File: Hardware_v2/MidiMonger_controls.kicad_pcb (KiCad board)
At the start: 2 copper layers, 40 x 110 mm, 31 parts, among them J10 Gate8_Out, J11 CV1_Out, J12 CV2_Out, J13 CV3_Out, J14 CV4_Out, J15 USB_B_Wurth, J16 MIDI_DIN, J2 Gate3_Out, J20 Conn_01x09_Female, J21 Conn_01x08_Female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

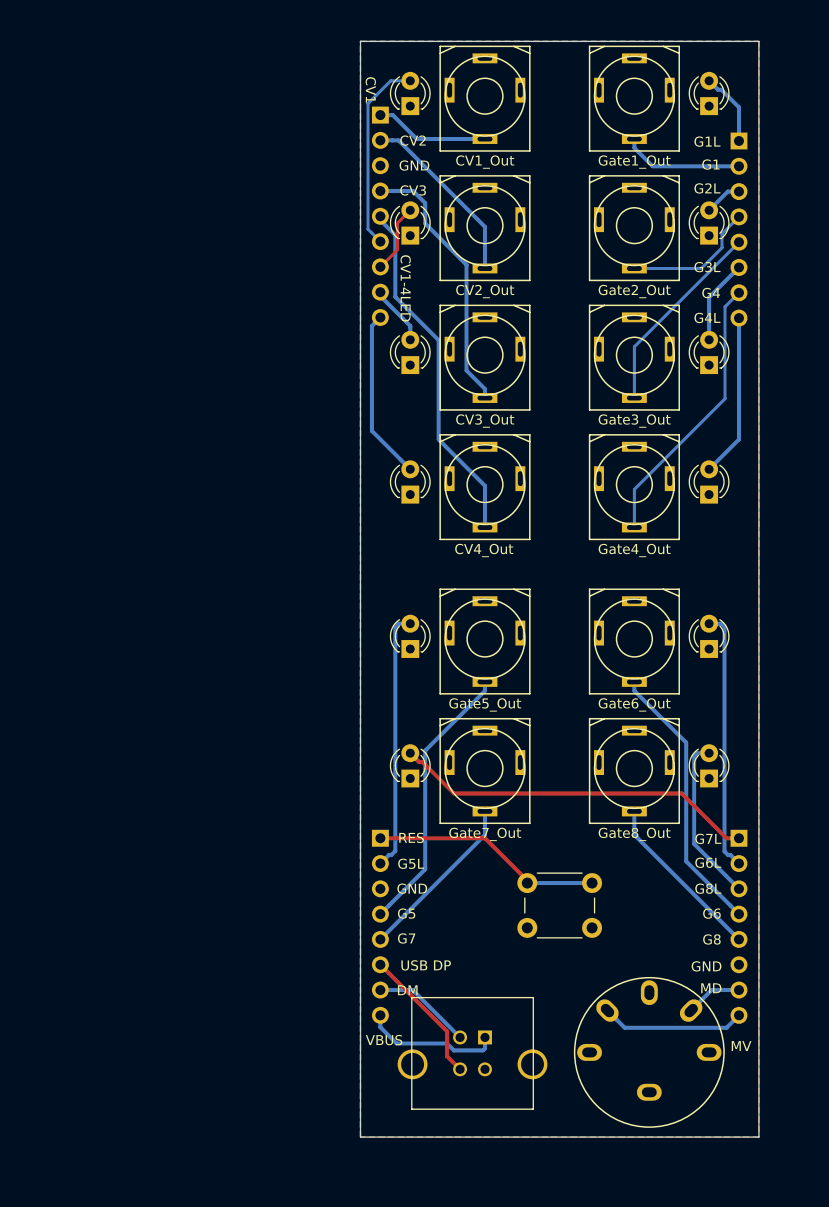
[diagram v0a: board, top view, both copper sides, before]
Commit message: Started Control layout
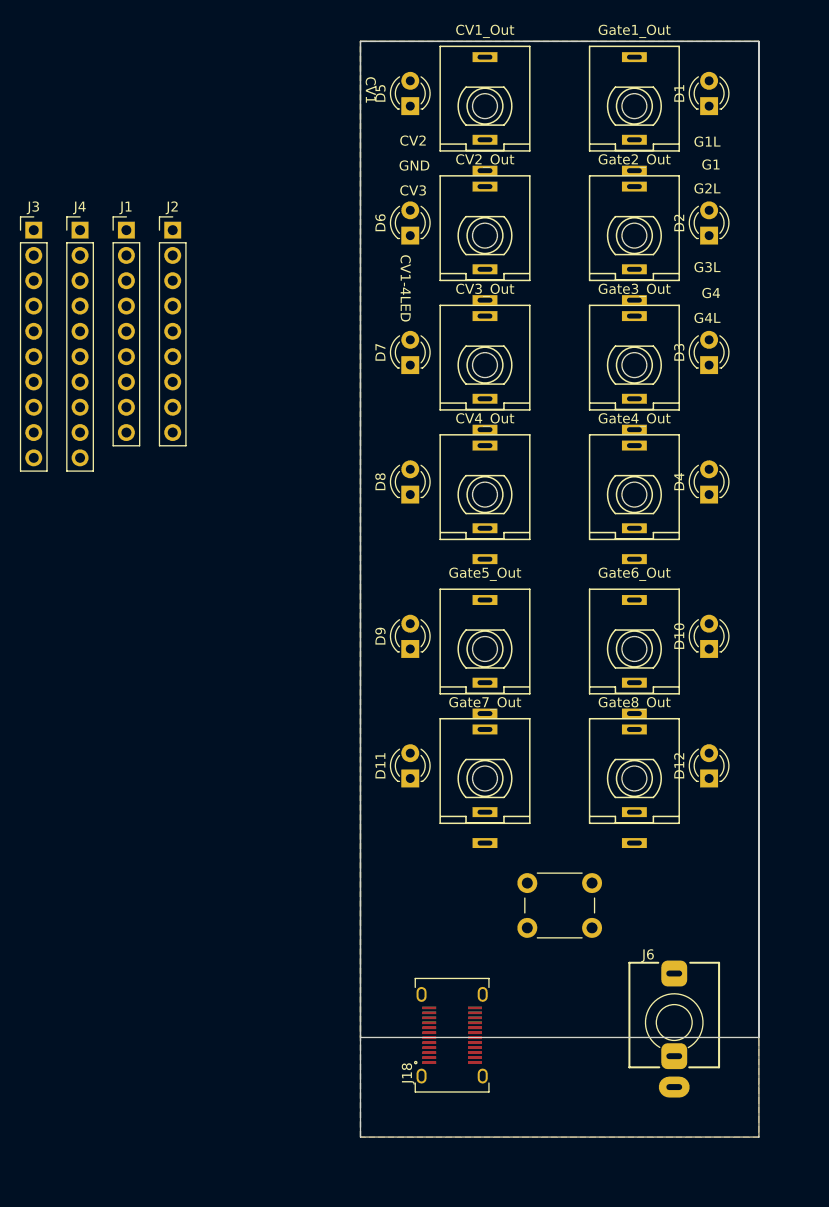
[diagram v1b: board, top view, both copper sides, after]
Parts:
- removed the J15 at (108.5, 140.0)
- removed the J16 at (125.0, 135.5)
- removed J20: Conn_01x09_Female, Socket_Strips:Socket_Strip_Straight_1x09_Pitch2.54mm
- removed J21, J22, J23: Conn_01x08_Female, Socket_Strips:Socket_Strip_Straight_1x08_Pitch2.54mm
- added J1: Conn_01x09_Male, Connector_PinHeader_2.54mm:PinHeader_1x09_P2.54mm_Vertical, F.Cu at (72.5, 59.0)
- added J18: USB_C_Receptacle, Custom_Footprints:USB_C_Receptacle_Amphenol_12401951E412A, F.Cu at (105.2, 139.8)
- added J2: Conn_01x09_Male, Connector_PinHeader_2.54mm:PinHeader_1x09_P2.54mm_Vertical, F.Cu at (77.2, 59.0)
- added J3: Conn_01x08_Male, Connector_PinHeader_2.54mm:PinHeader_1x10_P2.54mm_Vertical, F.Cu at (63.2, 59.0)
- added J4: Conn_01x08_Male, Connector_PinHeader_2.54mm:PinHeader_1x10_P2.54mm_Vertical, F.Cu at (67.8, 59.0)
- added J6: MIDI_IN, Custom_Footprints:Thonkiconn_Stereo-PJ366ST, F.Cu at (127.5, 138.5)
- D1, D10, D11, D12, D2, D3, D4, D5, D6, D7, D8, D9: footprint LEDs:LED_D3.0mm -> LED_THT:LED_D3.0mm_FlatTop
- J10: renamed from J7; footprint Custom_Footprints:Cliff_3.5mm_Stereo_Jack -> Custom_Footprints:THONKICONN_hole
- J11: renamed from J8; footprint Custom_Footprints:Cliff_3.5mm_Stereo_Jack -> Custom_Footprints:THONKICONN_hole
- J12: renamed from J9; footprint Custom_Footprints:Cliff_3.5mm_Stereo_Jack -> Custom_Footprints:THONKICONN_hole
- J13: renamed from J10; footprint Custom_Footprints:Cliff_3.5mm_Stereo_Jack -> Custom_Footprints:THONKICONN_hole
- J14: renamed from J11; footprint Custom_Footprints:Cliff_3.5mm_Stereo_Jack -> Custom_Footprints:THONKICONN_hole
- J15: renamed from J12; footprint Custom_Footprints:Cliff_3.5mm_Stereo_Jack -> Custom_Footprints:THONKICONN_hole
- J16: renamed from J13; footprint Custom_Footprints:Cliff_3.5mm_Stereo_Jack -> Custom_Footprints:THONKICONN_hole
- J17: renamed from J14; footprint Custom_Footprints:Cliff_3.5mm_Stereo_Jack -> Custom_Footprints:THONKICONN_hole
- J5: renamed from J2; footprint Custom_Footprints:Cliff_3.5mm_Stereo_Jack -> Custom_Footprints:THONKICONN_hole
- J7: renamed from J3; footprint Custom_Footprints:Cliff_3.5mm_Stereo_Jack -> Custom_Footprints:THONKICONN_hole
- J8: renamed from J4; footprint Custom_Footprints:Cliff_3.5mm_Stereo_Jack -> Custom_Footprints:THONKICONN_hole
- J9: renamed from J5; footprint Custom_Footprints:Cliff_3.5mm_Stereo_Jack -> Custom_Footprints:THONKICONN_hole
- SW1: value SW_Push -> Reset_Button
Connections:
- D1 pad 2: GATE1_LED_OUT -> /GATE1_LED_OUT
- D10 pad 2: GATE6_LED_OUT -> /GATE6_LED_OUT
- D11 pad 2: GATE7_LED_OUT -> /GATE7_LED_OUT
- D12 pad 2: GATE8_LED_OUT -> /GATE8_LED_OUT
- D2 pad 2: GATE2_LED_OUT -> /GATE2_LED_OUT
- D3 pad 2: GATE3_LED_OUT -> /GATE3_LED_OUT
- D4 pad 2: GATE4_LED_OUT -> /GATE4_LED_OUT
- D5 pad 2: CV1_LED_OUT -> /CV1_LED_OUT
- D6 pad 2: CV2_LED_OUT -> /CV2_LED_OUT
- D7 pad 2: CV3_LED_OUT -> /CV3_LED_OUT
- D8 pad 2: CV4_LED_OUT -> /CV4_LED_OUT
- D9 pad 2: GATE5_LED_OUT -> /GATE5_LED_OUT
- J10 pad 2: Net-(J7-Pad2) -> unconnected-(J10-Pad2)
- J10 pad 3: GATE5_OUT -> /GATE5_OUT
- J11 pad 2: Net-(J8-Pad2) -> unconnected-(J11-Pad2)
- J11 pad 3: GATE6_OUT -> /GATE6_OUT
- J12 pad 2: Net-(J9-Pad2) -> unconnected-(J12-Pad2)
- J12 pad 3: GATE7_OUT -> /GATE7_OUT
- J13 pad 2: Net-(J10-Pad2) -> unconnected-(J13-Pad2)
- J13 pad 3: GATE8_OUT -> /GATE8_OUT
- J14 pad 2: Net-(J11-Pad2) -> unconnected-(J14-Pad2)
- J14 pad 3: CV1_OUT -> /CV1_OUT
- J15 pad 2: Net-(J12-Pad2) -> unconnected-(J15-Pad2)
- J15 pad 3: CV2_OUT -> /CV2_OUT
- J16 pad 2: Net-(J13-Pad2) -> unconnected-(J16-Pad2)
- J16 pad 3: CV3_OUT -> /CV3_OUT
- J17 pad 2: Net-(J14-Pad2) -> unconnected-(J17-Pad2)
- J17 pad 3: CV4_OUT -> /CV4_OUT
- J5 pad 2: Net-(J2-Pad2) -> unconnected-(J5-Pad2)
- J5 pad 3: GATE3_OUT -> /GATE3_OUT
- J7 pad 2: Net-(J3-Pad2) -> unconnected-(J7-Pad2)
- J7 pad 3: GATE4_OUT -> /GATE4_OUT
- J8 pad 2: Net-(J4-Pad2) -> unconnected-(J8-Pad2)
- J8 pad 3: GATE1_OUT -> /GATE1_OUT
- J9 pad 2: Net-(J5-Pad2) -> unconnected-(J9-Pad2)
- J9 pad 3: GATE2_OUT -> /GATE2_OUT
- SW1 pad 1: RESET_SWITCH -> /NRST
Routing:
- net GATE7_LED_OUT: track 36.5 -> 0.00 mm
- net CV4_OUT: track 35.6 -> 0.00 mm
- net GATE4_OUT: track 27.9 -> 0.00 mm
- net GATE6_OUT: track 27.7 -> 0.00 mm
- net GATE5_OUT: track 27.7 -> 0.00 mm
- net CV3_OUT: track 27.1 -> 0.00 mm
- net GATE6_LED_OUT: track 26.2 -> 0.00 mm
- net GATE5_LED_OUT: track 26.2 -> 0.00 mm
- net RESET_SWITCH: track 23.4 -> 0.00 mm
- net GATE3_OUT: track 20.0 -> 0.00 mm
- net CV1_LED_OUT: track 19.6 -> 0.00 mm
- net CV2_OUT: track 18.3 -> 0.00 mm
- net GATE8_OUT: track 17.2 -> 0.00 mm
- net GATE7_OUT: track 17.2 -> 0.00 mm
- net CV4_LED_OUT: track 17.2 -> 0.00 mm
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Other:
- outline, holes or cut-outs redrawn
- net class Default removed
- board text removed: "DM"
- board text removed: "G5"
- board text removed: "G5L"
- board text removed: "G6"
- board text removed: "G6L"
- board text removed: "G7"
- board text removed: "G7L"
- board text removed: "G8"
- board text removed: "G8L"
- board text removed: "MD"
- board text removed: "MV"
- board text removed: "RES"
- board text removed: "USB DP"
- board text removed: "VBUS"

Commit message: Laying out panel
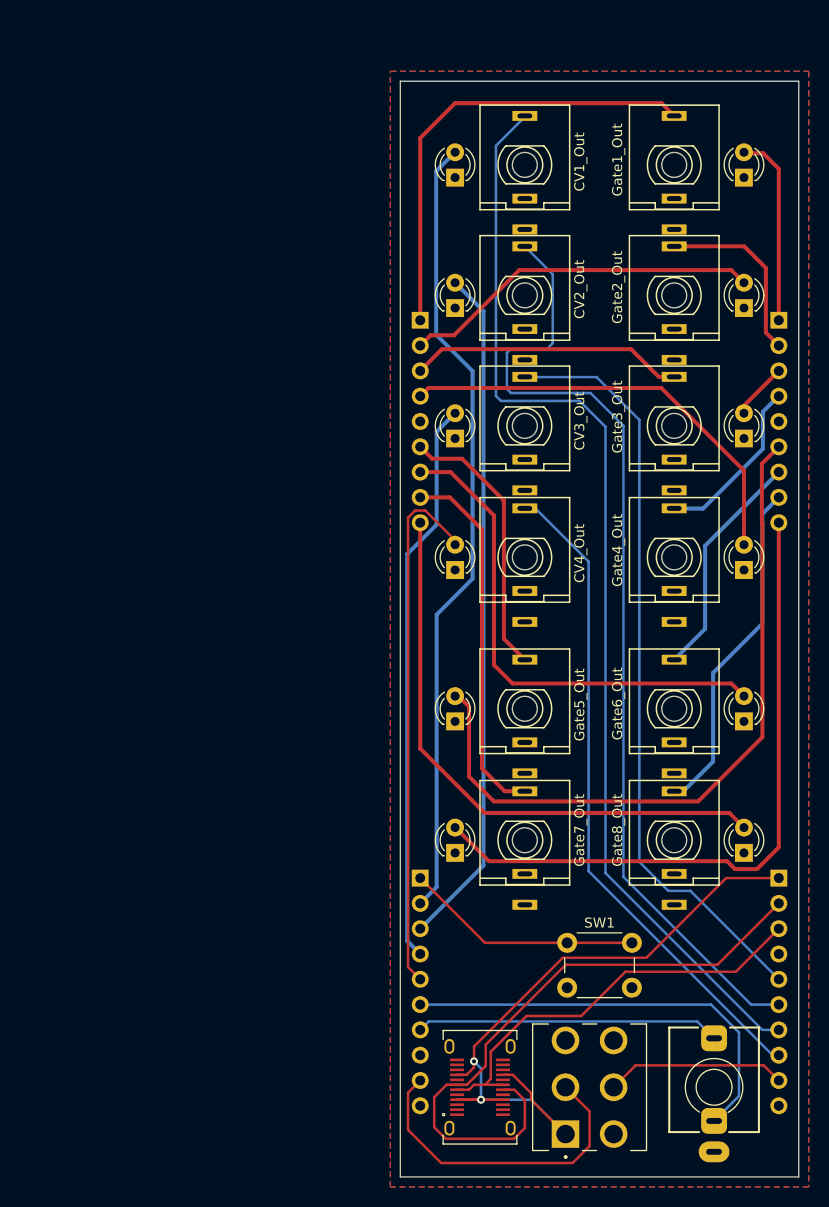
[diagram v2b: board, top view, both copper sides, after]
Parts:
- added SW4: SW_Push_DPDT, Custom_Footprints:100DP6T1B1M2QE_ON_ON_ON, F.Cu at (119.0, 145.0)
- D1, D10, D11, D12, D2, D3, D4, D5, D6, D7, D8, D9: footprint LED_THT:LED_D3.0mm_FlatTop -> Custom_Footprints:LED_D3.0mm
- J1, J2, J3, J4: moved to B.Cu
- SW1: footprint Buttons_Switches_THT:SW_PUSH_6mm -> Button_Switch_THT:SW_PUSH_6mm
- moved J4 95.7 mm to (138.0, 124.0), turned to 180 degrees
- moved J3 75.7 mm to (102.0, 124.0), turned to 180 degrees
- moved J2 61.5 mm to (138.0, 68.0), turned to 180 degrees
- moved J1 30.9 mm to (102.0, 68.0), turned to 180 degrees
- moved D8 7.74 mm to (105.5, 91.8)
- moved D11 7.66 mm to (105.5, 120.2)
- moved J6 7.63 mm to (131.5, 145.0)
- moved D7 7.58 mm to (105.5, 78.6)
- moved D6 7.50 mm to (105.5, 65.5)
- moved D9 7.50 mm to (105.5, 107.0)
- moved J17 7.46 mm to (112.5, 91.8)
- moved J7 7.46 mm to (127.5, 91.8)
- moved D5 7.42 mm to (105.5, 52.4)
- moved J12 7.38 mm to (112.5, 120.2)
- moved J13 7.38 mm to (127.5, 120.2)
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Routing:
- net /CV1_OUT: track 0.00 -> 110.3 mm
- net /CV2_OUT: track 0.00 -> 98.9 mm
- net /CV1_LED_OUT: track 0.00 -> 79.9 mm
- net /CV3_OUT: track 0.00 -> 76.5 mm
- net /USB_VBUS: track 0.00 -> 71.9 mm, vias 0 -> 2
- net /GATE5_LED_OUT: track 0.00 -> 71.9 mm
- net /CV2_LED_OUT: track 0.00 -> 69.2 mm
- net /GATE7_LED_OUT: track 0.00 -> 67.9 mm
- net /CV4_OUT: track 0.00 -> 66.6 mm
- net /USB_DM: track 0.00 -> 62.4 mm
- net /GATE8_LED_OUT: track 0.00 -> 58.5 mm
- net /CV3_LED_OUT: track 0.00 -> 56.8 mm
- net /CV4_LED_OUT: track 0.00 -> 53.6 mm
- net /GATE6_LED_OUT: track 0.00 -> 50.6 mm
- net /GATE1_OUT: track 0.00 -> 45.8 mm
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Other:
- outline, holes or cut-outs redrawn
- board text added: "Mountjoy Modular MIDI Monger Controls v2.0"
- board text removed: "CV1"
- board text removed: "CV1-4LED"
- board text removed: "CV2"
- board text removed: "CV3"
- board text removed: "G1"
- board text removed: "G1L"
- board text removed: "G2L"
- board text removed: "G3L"
- board text removed: "G4"
- board text removed: "G4L"
- board text removed: "GND"
- board text removed: "Mountjoy Modular MIDI Monger Controls v1.0"

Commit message: Hardware layout
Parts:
- moved J6 23.2 mm to (108.3, 146.0)
- moved SW4 13.1 mm to (132.1, 146.0)
- moved J18 12.0 mm to (120.0, 146.0), turned to -90 degrees
- moved SW1 2.05 mm to (116.8, 132.6)
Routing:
- net /USB_DM: track 62.4 -> 33.6 mm
- net /MIDI_VREF: track 43.1 -> 16.6 mm
- net /MIDI_DATA: track 30.6 -> 7.06 mm
- net /USB_VBUS: track 71.9 -> 51.0 mm, vias 2 -> 0
- net /MODE_SWITCH: track 18.1 -> 4.18 mm
- net /USB_DP: track 42.4 -> 28.9 mm, vias 0 -> 2
- net +5V: track 32.7 -> 29.1 mm
- net /NRST: track 23.9 -> 24.8 mm
- net /CV2_LED_OUT: track 69.2 -> 68.7 mm

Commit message: Gerbers prepared for manufacture
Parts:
- J1, J2: value Conn_01x09_Male -> Conn_01x09; footprint Connector_PinHeader_2.54mm:PinHeader_1x09_P2.54mm_Vertical -> Connector_PinSocket_2.54mm:PinSocket_1x09_P2.54mm_Vertical
- J3, J4: value Conn_01x08_Male -> Conn_01x10; footprint Connector_PinHeader_2.54mm:PinHeader_1x10_P2.54mm_Vertical -> Connector_PinSocket_2.54mm:PinSocket_1x10_P2.54mm_Vertical
- SW4: value SW_Push_DPDT -> Host_Device_Switch
- moved SW4 0.60 mm to (131.5, 146.0)
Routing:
- net /MODE_SWITCH: track 4.18 -> 4.78 mm
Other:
- board text added: "Mountjoy Modular MIDIMonger Controls v2.0"
- board text removed: "Mountjoy Modular MIDI Monger Controls v2.0"
